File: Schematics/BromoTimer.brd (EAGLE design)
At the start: 89.8 x 66 mm, 28 parts, among them IC1 PIC16F687, IC2 7805TV, K1 G2R2A, K2 G2R2A, Q1 BC548B, Q2 BC548B, Q3 BC548B, X1 AC_IN, X4 22-23-2031, X5 AC_OUT

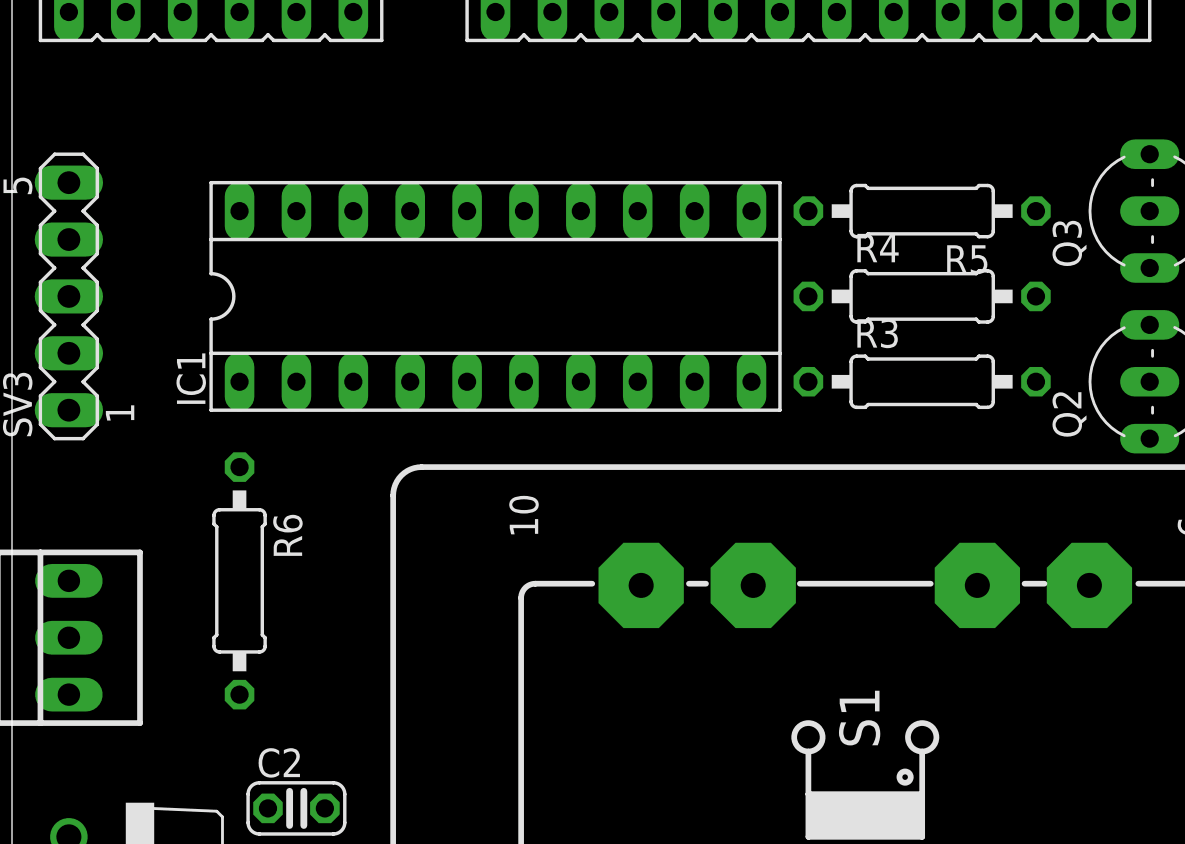
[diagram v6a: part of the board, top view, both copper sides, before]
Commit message: Adjusted some positions in the board layout
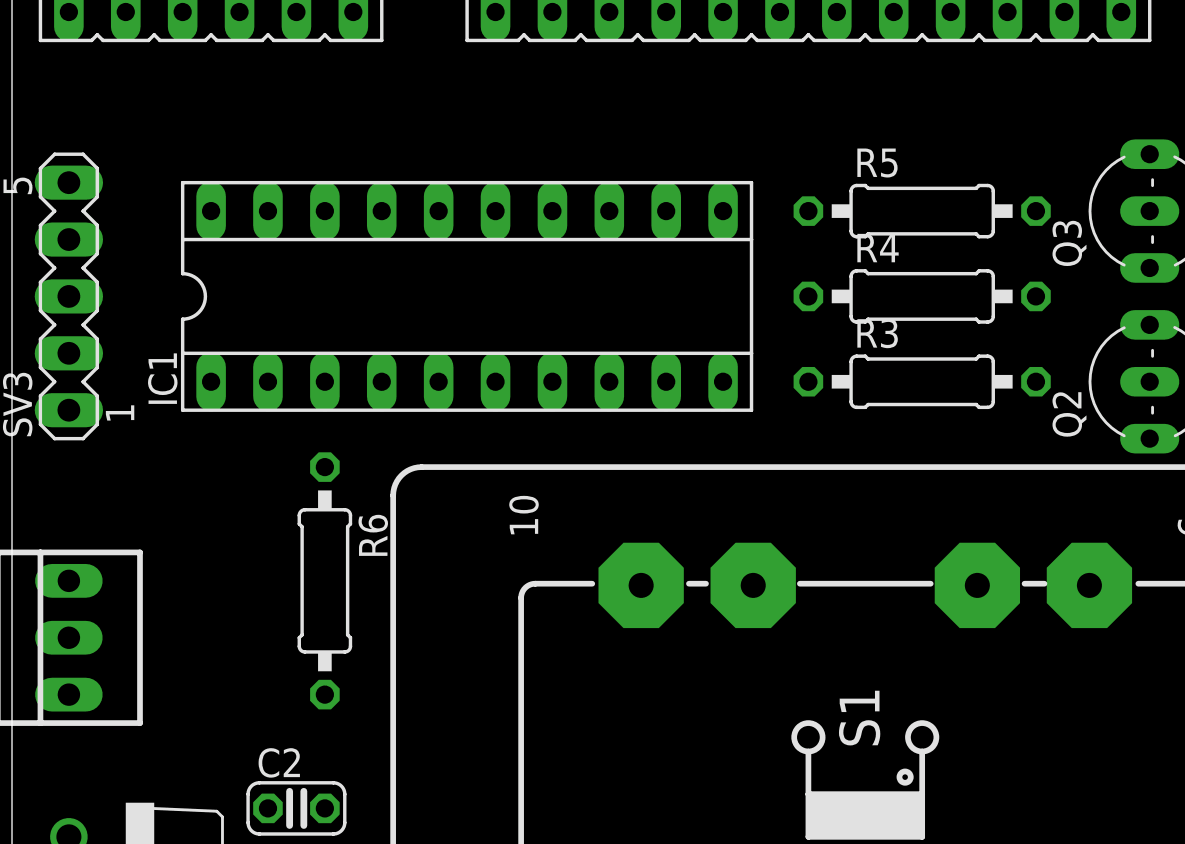
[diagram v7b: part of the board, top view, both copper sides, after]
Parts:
- moved R6 3.81 mm to (14.0, 38.1)
- moved IC1 1.27 mm to (20.3, 50.8)
- turned R5 to 0 degrees
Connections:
- net N$17: now also R5.1; no longer R5.2
- net N$18: now also R5.2; no longer R5.1
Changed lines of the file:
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@@
 <wire x1="89.84" y1="66.03" x2="0" y2="66.03" width="0" layer="20"/>
 <wire x1="0" y1="66.03" x2="0" y2="0" width="0" layer="20"/>
+<dimension x1="0" y1="66.0273" x2="89.8398" y2="66.0273" x3="44.9199" y3="71.12" layer="20"/>
+<dimension x1="0" y1="0" x2="0" y2="66.04" x3="-5.08" y3="33.02" layer="20"/>
 </plain>
 <attributes>
@@
 </autorouter>
 <elements>
-<element name="IC1" library="ic-package" package="SOCKET-20" value="PIC16F687" x="21.59" y="50.8"/>
+<element name="IC1" library="ic-package" package="SOCKET-20" value="PIC16F687" x="20.32" y="50.8"/>
 <element name="SV1" library="con-lsta" package="FE06" value="ENCODER" x="8.89" y="63.5">
 <attribute name="OC_NEWARK" value="unknown" x="62.23" y="3.81" size="1.778" layer="27" display="off"/>
@@
 <element name="D3" library="diode" package="DO41-10" value="1N4004" x="2.54" y="21.59" rot="R90"/>
 <element name="Q3" library="transistor-npn" package="TO92-EBC" value="BC548B" x="49.53" y="54.61" rot="R90"/>
-<element name="R5" library="rcl" package="0207/10" value="" x="40.64" y="54.61" rot="R180"/>
+<element name="R5" library="rcl" package="0207/10" value="" x="40.64" y="54.61"/>
 <element name="X4" library="con-molex" package="22-23-2031" value="22-23-2031" x="2.54" y="35.56" rot="R90">
 <attribute name="OC_NEWARK" value="30C0862" x="2.54" y="35.56" size="1.778" layer="27" rot="R90" display="off"/>
@@
 <element name="TR1" library="trafo" package="EI38-1" value="220/12" x="38.1" y="25.4" rot="R90"/>
 <element name="C3" library="rcl" package="C050-050X075" value="330n" x="12.7" y="20.32" rot="R90"/>
-<element name="R6" library="rcl" package="0207/10" value="470" x="10.16" y="38.1" rot="R270"/>
+<element name="R6" library="rcl" package="0207/10" value="470" x="13.97" y="38.1" rot="R270"/>
 <element name="X1" library="con-phoenix-508" package="MKDSN1,5/3-5,08" value="AC_IN" x="40.64" y="2.54" rot="R180">
 <attribute name="OC_NEWARK" value="70R0299" x="40.64" y="2.54" size="1.778" layer="27" rot="R180" display="off"/>
@@
 <contactref element="D3" pad="A"/>
 <wire x1="24.13" y1="63.5" x2="59.69" y2="62.865" width="0" layer="19" extent="1-1"/>
-<wire x1="10.16" y1="54.61" x2="24.13" y2="63.5" width="0" layer="19" extent="1-1"/>
-<wire x1="2.54" y1="48.26" x2="10.16" y2="54.61" width="0" layer="19" extent="1-1"/>
+<wire x1="8.89" y1="54.61" x2="24.13" y2="63.5" width="0" layer="19" extent="1-1"/>
+<wire x1="2.54" y1="48.26" x2="8.89" y2="54.61" width="0" layer="19" extent="1-1"/>
 <wire x1="2.54" y1="26.67" x2="2.54" y2="48.26" width="0" layer="19" extent="1-1"/>
 <wire x1="7.62" y1="25.4" x2="2.54" y2="26.67" width="0" layer="19" extent="1-1"/>
@@
 <wire x1="2.54" y1="63.5" x2="21.59" y2="63.5" width="0" layer="19" extent="1-1"/>
 <wire x1="2.54" y1="50.8" x2="2.54" y2="63.5" width="0" layer="19" extent="1-1"/>
-<wire x1="10.16" y1="46.99" x2="2.54" y2="50.8" width="0" layer="19" extent="1-1"/>
-<wire x1="2.54" y1="38.1" x2="10.16" y2="46.99" width="0" layer="19" extent="1-1"/>
+<wire x1="8.89" y1="46.99" x2="2.54" y2="50.8" width="0" layer="19" extent="1-1"/>
+<wire x1="2.54" y1="38.1" x2="8.89" y2="46.99" width="0" layer="19" extent="1-1"/>
 <wire x1="7.62" y1="22.86" x2="2.54" y2="38.1" width="0" layer="19" extent="1-1"/>
 <wire x1="12.7" y1="22.86" x2="7.62" y2="22.86" width="0" layer="19" extent="1-1"/>
@@
 <contactref element="SV2" pad="4"/>
 <contactref element="IC1" pad="15"/>
-<wire x1="22.86" y1="54.61" x2="29.21" y2="63.5" width="0" layer="19" extent="1-1"/>
+<wire x1="21.59" y1="54.61" x2="29.21" y2="63.5" width="0" layer="19" extent="1-1"/>
 </signal>
 <signal name="RW">
 <contactref element="SV2" pad="5"/>
 <contactref element="IC1" pad="14"/>
-<wire x1="25.4" y1="54.61" x2="31.75" y2="63.5" width="0" layer="19" extent="1-1"/>
+<wire x1="24.13" y1="54.61" x2="31.75" y2="63.5" width="0" layer="19" extent="1-1"/>
 </signal>
 <signal name="EN">
 <contactref element="SV2" pad="6"/>
 <contactref element="IC1" pad="16"/>
-<wire x1="20.32" y1="54.61" x2="34.29" y2="63.5" width="0" layer="19" extent="1-1"/>
+<wire x1="19.05" y1="54.61" x2="34.29" y2="63.5" width="0" layer="19" extent="1-1"/>
 </signal>
 <signal name="B0">
 <contactref element="SV2" pad="7"/>
 <contactref element="IC1" pad="13"/>
-<wire x1="27.94" y1="54.61" x2="36.83" y2="63.5" width="0" layer="19" extent="1-1"/>
+<wire x1="26.67" y1="54.61" x2="36.83" y2="63.5" width="0" layer="19" extent="1-1"/>
 </signal>
 <signal name="B1">
 <contactref element="SV2" pad="8"/>
 <contactref element="IC1" pad="12"/>
-<wire x1="30.48" y1="54.61" x2="39.37" y2="63.5" width="0" layer="19" extent="1-1"/>
+<wire x1="29.21" y1="54.61" x2="39.37" y2="63.5" width="0" layer="19" extent="1-1"/>
 </signal>
 <signal name="B2">
 <contactref element="SV2" pad="9"/>
 <contactref element="IC1" pad="11"/>
-<wire x1="33.02" y1="54.61" x2="41.91" y2="63.5" width="0" layer="19" extent="1-1"/>
+<wire x1="31.75" y1="54.61" x2="41.91" y2="63.5" width="0" layer="19" extent="1-1"/>
 </signal>
 <signal name="B3">
 <contactref element="SV2" pad="10"/>
 <contactref element="IC1" pad="10"/>
-<wire x1="33.02" y1="46.99" x2="44.45" y2="63.5" width="0" layer="19" extent="1-1"/>
+<wire x1="31.75" y1="46.99" x2="44.45" y2="63.5" width="0" layer="19" extent="1-1"/>
 </signal>
 <signal name="N$1">
@@
 <contactref element="SV1" pad="2"/>
 <contactref element="IC1" pad="8"/>
-<wire x1="5.08" y1="63.5" x2="27.94" y2="46.99" width="0" layer="19" extent="1-1"/>
+<wire x1="5.08" y1="63.5" x2="26.67" y2="46.99" width="0" layer="19" extent="1-1"/>
 </signal>
 <signal name="L2">
 <contactref element="SV1" pad="3"/>
 <contactref element="IC1" pad="9"/>
-<wire x1="7.62" y1="63.5" x2="30.48" y2="46.99" width="0" layer="19" extent="1-1"/>
+<wire x1="7.62" y1="63.5" x2="29.21" y2="46.99" width="0" layer="19" extent="1-1"/>
 </signal>
 <signal name="SW">
 <contactref element="SV1" pad="4"/>
 <contactref element="IC1" pad="2"/>
-<wire x1="12.7" y1="46.99" x2="10.16" y2="63.5" width="0" layer="19" extent="1-1"/>
+<wire x1="11.43" y1="46.99" x2="10.16" y2="63.5" width="0" layer="19" extent="1-1"/>
 </signal>
 <signal name="A">
@@
 <contactref element="IC1" pad="19"/>
 <contactref element="SV3" pad="4"/>
-<wire x1="12.7" y1="54.61" x2="12.7" y2="63.5" width="0" layer="19" extent="1-1"/>
-<wire x1="2.54" y1="53.34" x2="12.7" y2="54.61" width="0" layer="19" extent="1-1"/>
+<wire x1="11.43" y1="54.61" x2="12.7" y2="63.5" width="0" layer="19" extent="1-1"/>
+<wire x1="2.54" y1="53.34" x2="11.43" y2="54.61" width="0" layer="19" extent="1-1"/>
 </signal>
 <signal name="B">
@@
 <contactref element="IC1" pad="18"/>
 <contactref element="SV3" pad="5"/>
-<wire x1="15.24" y1="54.61" x2="15.24" y2="63.5" width="0" layer="19" extent="1-1"/>
-<wire x1="2.54" y1="55.88" x2="15.24" y2="54.61" width="0" layer="19" extent="1-1"/>
+<wire x1="13.97" y1="54.61" x2="15.24" y2="63.5" width="0" layer="19" extent="1-1"/>
+<wire x1="2.54" y1="55.88" x2="13.97" y2="54.61" width="0" layer="19" extent="1-1"/>
 </signal>
 <signal name="N$4">
@@
 <contactref element="R3" pad="1"/>
 <contactref element="IC1" pad="7"/>
-<wire x1="25.4" y1="46.99" x2="35.56" y2="46.99" width="0" layer="19" extent="1-1"/>
+<wire x1="24.13" y1="46.99" x2="35.56" y2="46.99" width="0" layer="19" extent="1-1"/>
 </signal>
 <signal name="N$14">
 <contactref element="IC1" pad="6"/>
 <contactref element="R4" pad="1"/>
-<wire x1="22.86" y1="46.99" x2="35.56" y2="50.8" width="0" layer="19" extent="1-1"/>
+<wire x1="21.59" y1="46.99" x2="35.56" y2="50.8" width="0" layer="19" extent="1-1"/>
 </signal>
 <signal name="N$15">
 <contactref element="SV3" pad="1"/>
 <contactref element="IC1" pad="4"/>
-<wire x1="2.54" y1="45.72" x2="17.78" y2="46.99" width="0" layer="19" extent="1-1"/>
+<wire x1="2.54" y1="45.72" x2="16.51" y2="46.99" width="0" layer="19" extent="1-1"/>
 </signal>
 <signal name="N$17">
-<contactref element="R5" pad="2"/>
+<contactref element="R5" pad="1"/>
 <contactref element="IC1" pad="5"/>
-<wire x1="20.32" y1="46.99" x2="35.56" y2="54.61" width="0" layer="19" extent="1-1"/>
+<wire x1="19.05" y1="46.99" x2="35.56" y2="54.61" width="0" layer="19" extent="1-1"/>
 </signal>
 <signal name="N$13">
 <contactref element="IC1" pad="17"/>
 <contactref element="X4" pad="2"/>
-<wire x1="2.54" y1="35.56" x2="17.78" y2="54.61" width="0" layer="19" extent="1-1"/>
+<wire x1="2.54" y1="35.56" x2="16.51" y2="54.61" width="0" layer="19" extent="1-1"/>
 </signal>
 <signal name="N$18">
 <contactref element="Q3" pad="B"/>
-<contactref element="R5" pad="1"/>
+<contactref element="R5" pad="2"/>
 <wire x1="45.72" y1="54.61" x2="50.8" y2="54.61" width="0" layer="19" extent="1-1"/>
 </signal>
@@
 <contactref element="IC1" pad="3"/>
 <contactref element="R6" pad="1"/>
-<wire x1="10.16" y1="43.18" x2="15.24" y2="46.99" width="0" layer="19" extent="1-1"/>
+<wire x1="13.97" y1="43.18" x2="13.97" y2="46.99" width="0" layer="19" extent="1-1"/>
 </signal>
 <signal name="N$21">
 <contactref element="X4" pad="1"/>
 <contactref element="R6" pad="2"/>
-<wire x1="2.54" y1="33.02" x2="10.16" y2="33.02" width="0" layer="19" extent="1-1"/>
+<wire x1="2.54" y1="33.02" x2="13.97" y2="33.02" width="0" layer="19" extent="1-1"/>
 </signal>
 <signal name="N$2">

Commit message: Routing nearly done
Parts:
- moved D1 2.84 mm to (61.0, 52.1)
- moved D2 2.84 mm to (61.0, 54.6)
- moved SV3 2.84 mm to (5.08, 49.5)
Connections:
- net +5V: now also D1.C, D2.C, K1.1, K2.1
- net V+: no longer D1.C, D2.C, K1.1, K2.1
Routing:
- net GND: track 0.00 -> 220.3 mm
- net +5V: track 0.00 -> 142.8 mm
- net AC2: track 0.00 -> 80.3 mm
- net AC1: track 0.00 -> 45.0 mm
- net N$7: track 0.00 -> 44.6 mm
- net N$2: track 0.00 -> 43.7 mm
- net N$12: track 0.00 -> 39.6 mm
- net V+: track 0.00 -> 37.5 mm
- net N$6: track 0.00 -> 37.0 mm
- net N$19: track 0.00 -> 31.6 mm
- net N$13: track 0.00 -> 31.1 mm
- net SW: track 0.00 -> 28.6 mm
- net A: track 0.00 -> 28.0 mm
- net B: track 0.00 -> 25.5 mm
- net B3: track 0.00 -> 23.3 mm
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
